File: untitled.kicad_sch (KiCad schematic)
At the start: 4 parts, among them J4 Conn_01x14_MountingPin, J5 AVR-ISP-6, J6 Conn_01x14_MountingPin, U4 ATmega328P-P

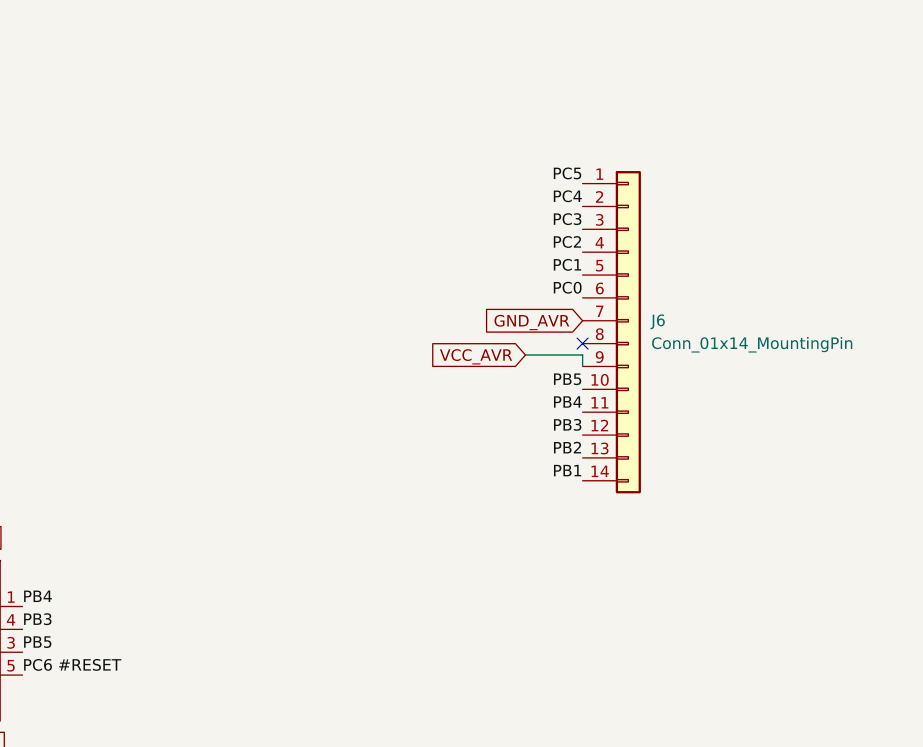
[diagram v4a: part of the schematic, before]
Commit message: changed MCP header into two headers mirroring part
also rearanged components on board
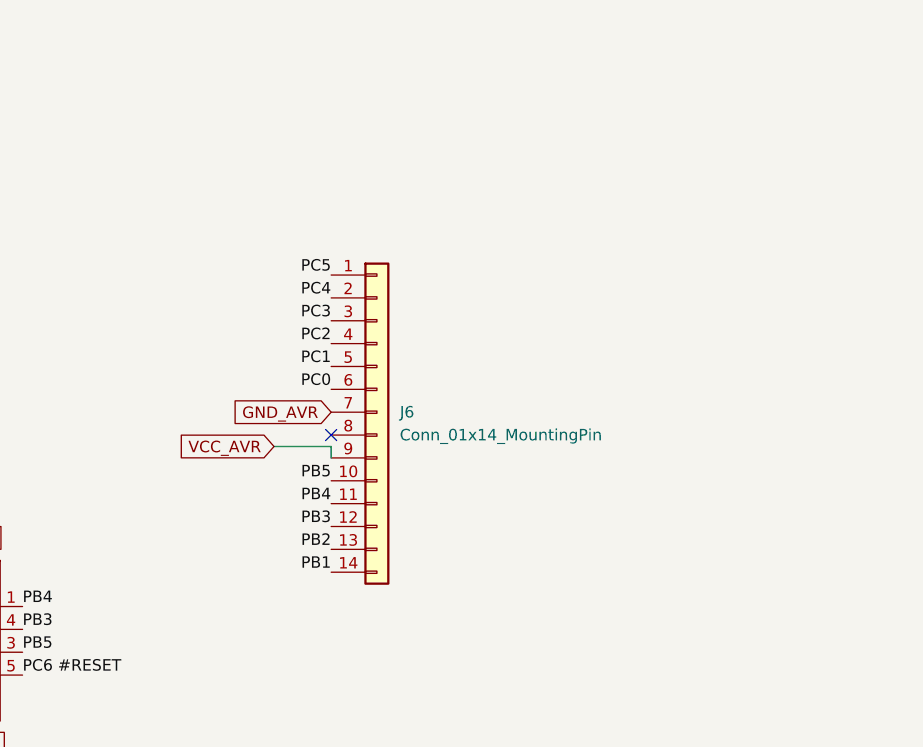
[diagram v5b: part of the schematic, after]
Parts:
- J4, J6: footprint (none) -> Connector_PinHeader_2.54mm:PinHeader_1x14_P2.54mm_Vertical
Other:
- moved on the sheet: J6
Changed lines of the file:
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@@
 	)
 	(no_connect
-		(at 246.38 67.31)
+		(at 218.44 77.47)
 	)
 	(wire
@@
 	(wire
 		(pts
-			(xy 240.03 68.58) (xy 246.38 68.58)
+			(xy 212.09 78.74) (xy 218.44 78.74)
 		)
 		(stroke
@@
 	(wire
 		(pts
-			(xy 246.38 68.58) (xy 246.38 69.85)
+			(xy 218.44 78.74) (xy 218.44 80.01)
 		)
 		(stroke
@@
 	)
 	(label "PB5"
-		(at 246.38 72.39 180)
+		(at 218.44 82.55 180)
 		(fields_autoplaced yes)
 		(effects
@@
 	)
 	(label "PB2"
-		(at 246.38 80.01 180)
+		(at 218.44 90.17 180)
 		(fields_autoplaced yes)
 		(effects
@@
 	)
 	(label "PC5"
-		(at 246.38 49.53 180)
+		(at 218.44 59.69 180)
 		(fields_autoplaced yes)
 		(effects
@@
 	)
 	(label "PB4"
-		(at 246.38 74.93 180)
+		(at 218.44 85.09 180)
 		(fields_autoplaced yes)
 		(effects
@@
 	)
 	(label "PC1"
-		(at 246.38 59.69 180)
+		(at 218.44 69.85 180)
 		(fields_autoplaced yes)
 		(effects
@@
 	)
 	(label "PB3"
-		(at 246.38 77.47 180)
+		(at 218.44 87.63 180)
 		(fields_autoplaced yes)
 		(effects
@@
 	)
 	(label "PC4"
-		(at 246.38 52.07 180)
+		(at 218.44 62.23 180)
 		(fields_autoplaced yes)
 		(effects
@@
 	)
 	(label "PC0"
-		(at 246.38 62.23 180)
+		(at 218.44 72.39 180)
 		(fields_autoplaced yes)
 		(effects
@@
 	)
 	(label "PB1"
-		(at 246.38 82.55 180)
+		(at 218.44 92.71 180)
 		(fields_autoplaced yes)
 		(effects
@@
 	)
 	(label "PC3"
-		(at 246.38 54.61 180)
+		(at 218.44 64.77 180)
 		(fields_autoplaced yes)
 		(effects
@@
 	)
 	(label "PC2"
-		(at 246.38 57.15 180)
+		(at 218.44 67.31 180)
 		(fields_autoplaced yes)
 		(effects
@@
 	(global_label "VCC_AVR"
 		(shape input)
-		(at 240.03 68.58 180)
+		(at 212.09 78.74 180)
 		(fields_autoplaced yes)
 		(effects
@@
 		)
 		(property "Intersheetrefs" "${INTERSHEET_REFS}"
-			(at 229.0014 68.58 0)
+			(at 201.0614 78.74 0)
 			(effects
 				(font
@@
 	(global_label "GND_AVR"
 		(shape input)
-		(at 246.38 64.77 180)
+		(at 218.44 74.93 180)
 		(fields_autoplaced yes)
 		(effects
@@
 		)
 		(property "Intersheetrefs" "${INTERSHEET_REFS}"
-			(at 235.1095 64.77 0)
+			(at 207.1695 74.93 0)
 			(effects
 				(font
@@
 	(symbol
 		(lib_id "Connector_Generic:Conn_01x14")
-		(at 251.46 64.77 0)
+		(at 223.52 74.93 0)
 		(unit 1)
 		(exclude_from_sim no)
@@
 		(fields_autoplaced yes)
 		(property "Reference" "J6"
-			(at 254 64.7699 0)
+			(at 226.06 74.9299 0)
 			(effects
 				(font
@@
 		)
 		(property "Value" "Conn_01x14_MountingPin"
-			(at 254 67.3099 0)
+			(at 226.06 77.4699 0)
 			(effects
 				(font
@@
 			)
 		)
-		(property "Footprint" ""
-			(at 251.46 64.77 0)
+		(property "Footprint" "Connector_PinHeader_2.54mm:PinHeader_1x14_P2.54mm_Vertical"
+			(at 223.52 74.93 0)
 			(effects
 				(font
@@
 		)
 		(property "Datasheet" "~"
-			(at 251.46 64.77 0)
+			(at 223.52 74.93 0)
 			(effects
 				(font
@@
 		)
 		(property "Description" "Generic connector, single row, 01x14, script generated (kicad-library-utils/schlib/autogen/connector/)"
-			(at 251.46 64.77 0)
+			(at 223.52 74.93 0)
 			(effects
 				(font
@@
 			)
 		)
-		(property "Footprint" ""
+		(property "Footprint" "Connector_PinHeader_2.54mm:PinHeader_1x14_P2.54mm_Vertical"
 			(at 138.43 73.66 0)
 			(effects
